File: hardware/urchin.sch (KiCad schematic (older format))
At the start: 19 parts, among them IC1 ATMEGA328PB-A, IC2 ATTINY85-S, P1 CONN_02X03, P2 USB_OTG, U1 CH340G, Y1 12M

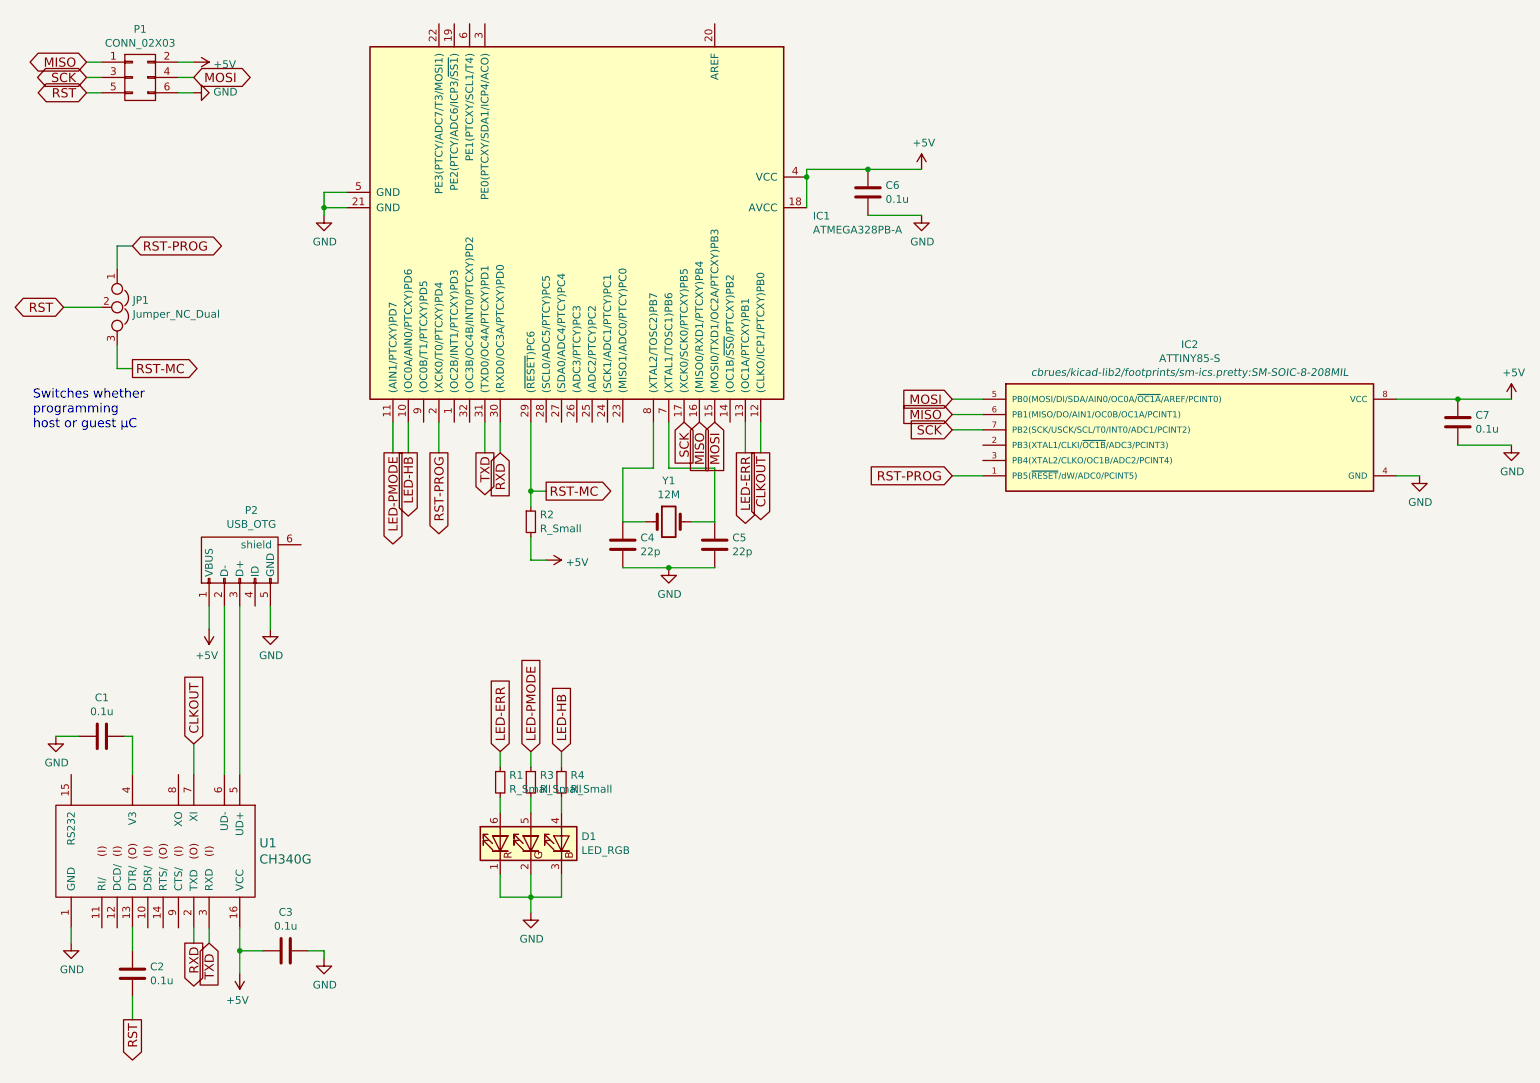
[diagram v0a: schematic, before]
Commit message: Adding new 100uF reservoir capacitor.
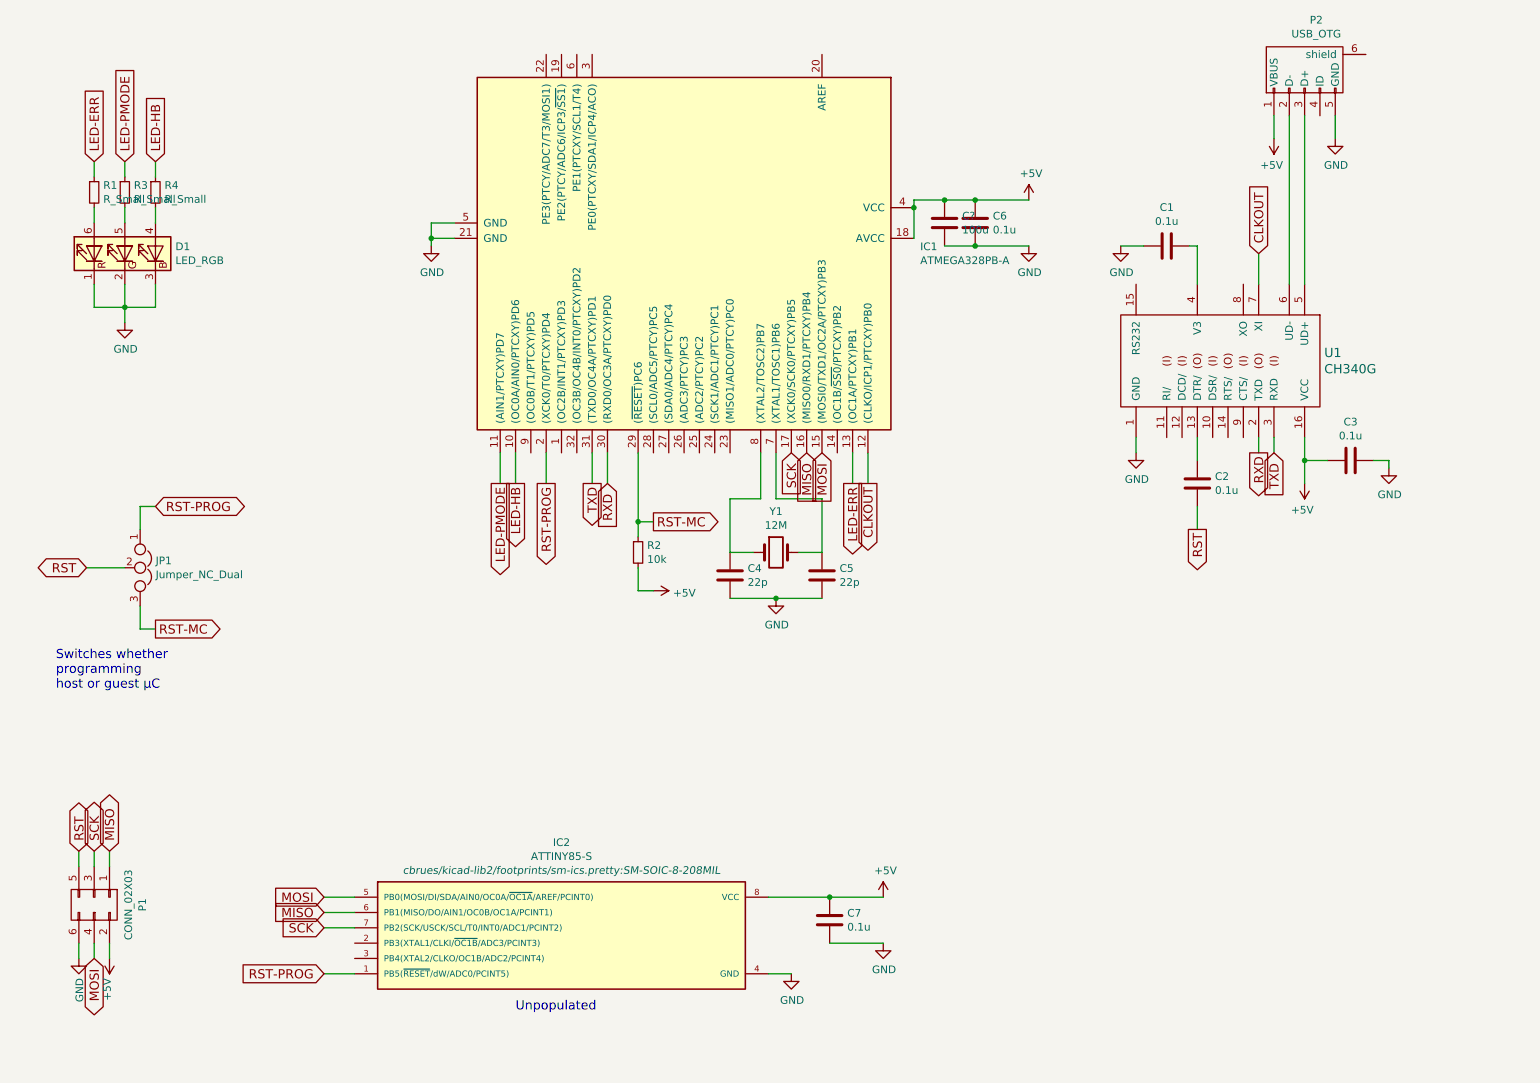
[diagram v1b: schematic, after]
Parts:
- added C?: 100u, symbol C
- R2: value R_Small -> 10k
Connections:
- net +5V: now also C?.1
- net GND: now also C?.2
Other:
- note added: "Unpopulated"
- moved on the sheet: C1, C2, C3, C4, C5, C6, C7, D1, IC1, IC2, JP1, P1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
